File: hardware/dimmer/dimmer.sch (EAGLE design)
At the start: 34 parts, among them IC1 MEGA328PU, IC2 RFM12, IC3 7812L, IC4 LP2950Z, K1 G5LE, T1 BC547, T2 BC547, X1 AC In, X2 DIM Out, X3 AC Out

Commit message: label added
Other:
- note added: "Date: 06.04.2014"
- note removed: "Date: 05.04.2014"
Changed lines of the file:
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@@
 <frame x1="-81.28" y1="-104.14" x2="99.06" y2="91.44" columns="8" rows="5" layer="97"/>
 <text x="12.7" y="-76.2" size="3.81" layer="97">smarthomatic Dimmer</text>
-<text x="63.5" y="-81.28" size="2.1844" layer="97">Date: 05.04.2014</text>
+<text x="63.5" y="-81.28" size="2.1844" layer="97">Date: 06.04.2014</text>
 <text x="12.7" y="-81.28" size="2.1844" layer="97">Rev 1.0</text>
 <text x="12.7" y="-86.36" size="2.1844" layer="97">Copyright (c) Uwe Freese, www.smarthomatic.org</text>

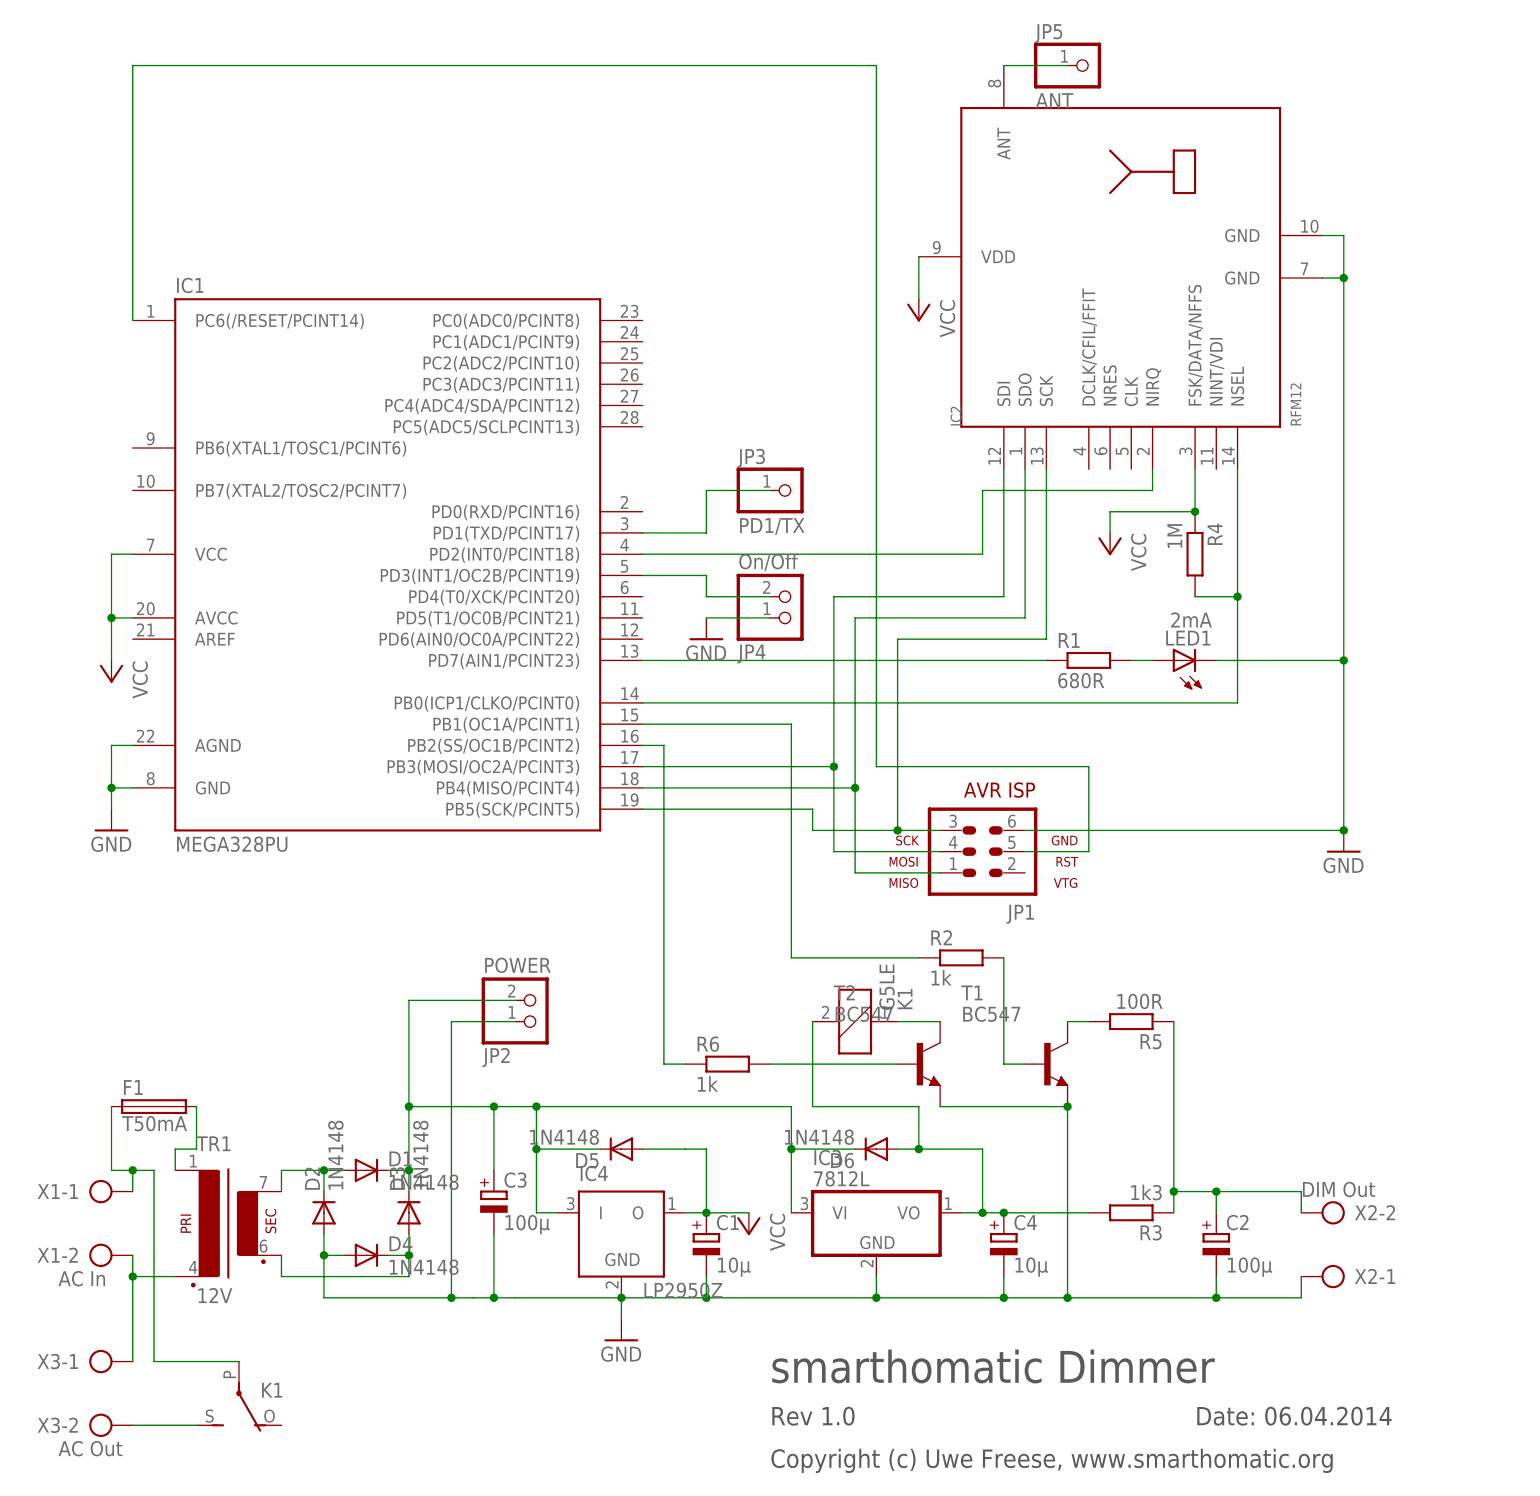
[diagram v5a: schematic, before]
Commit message: Add 220nF capacitors at ATMega + RFM12. Use more powerful transformer, also 15V now. Use smaller relay. Use 15V transformer output voltage for relay instead of regulated voltage from 78L12. Smaller PCB.
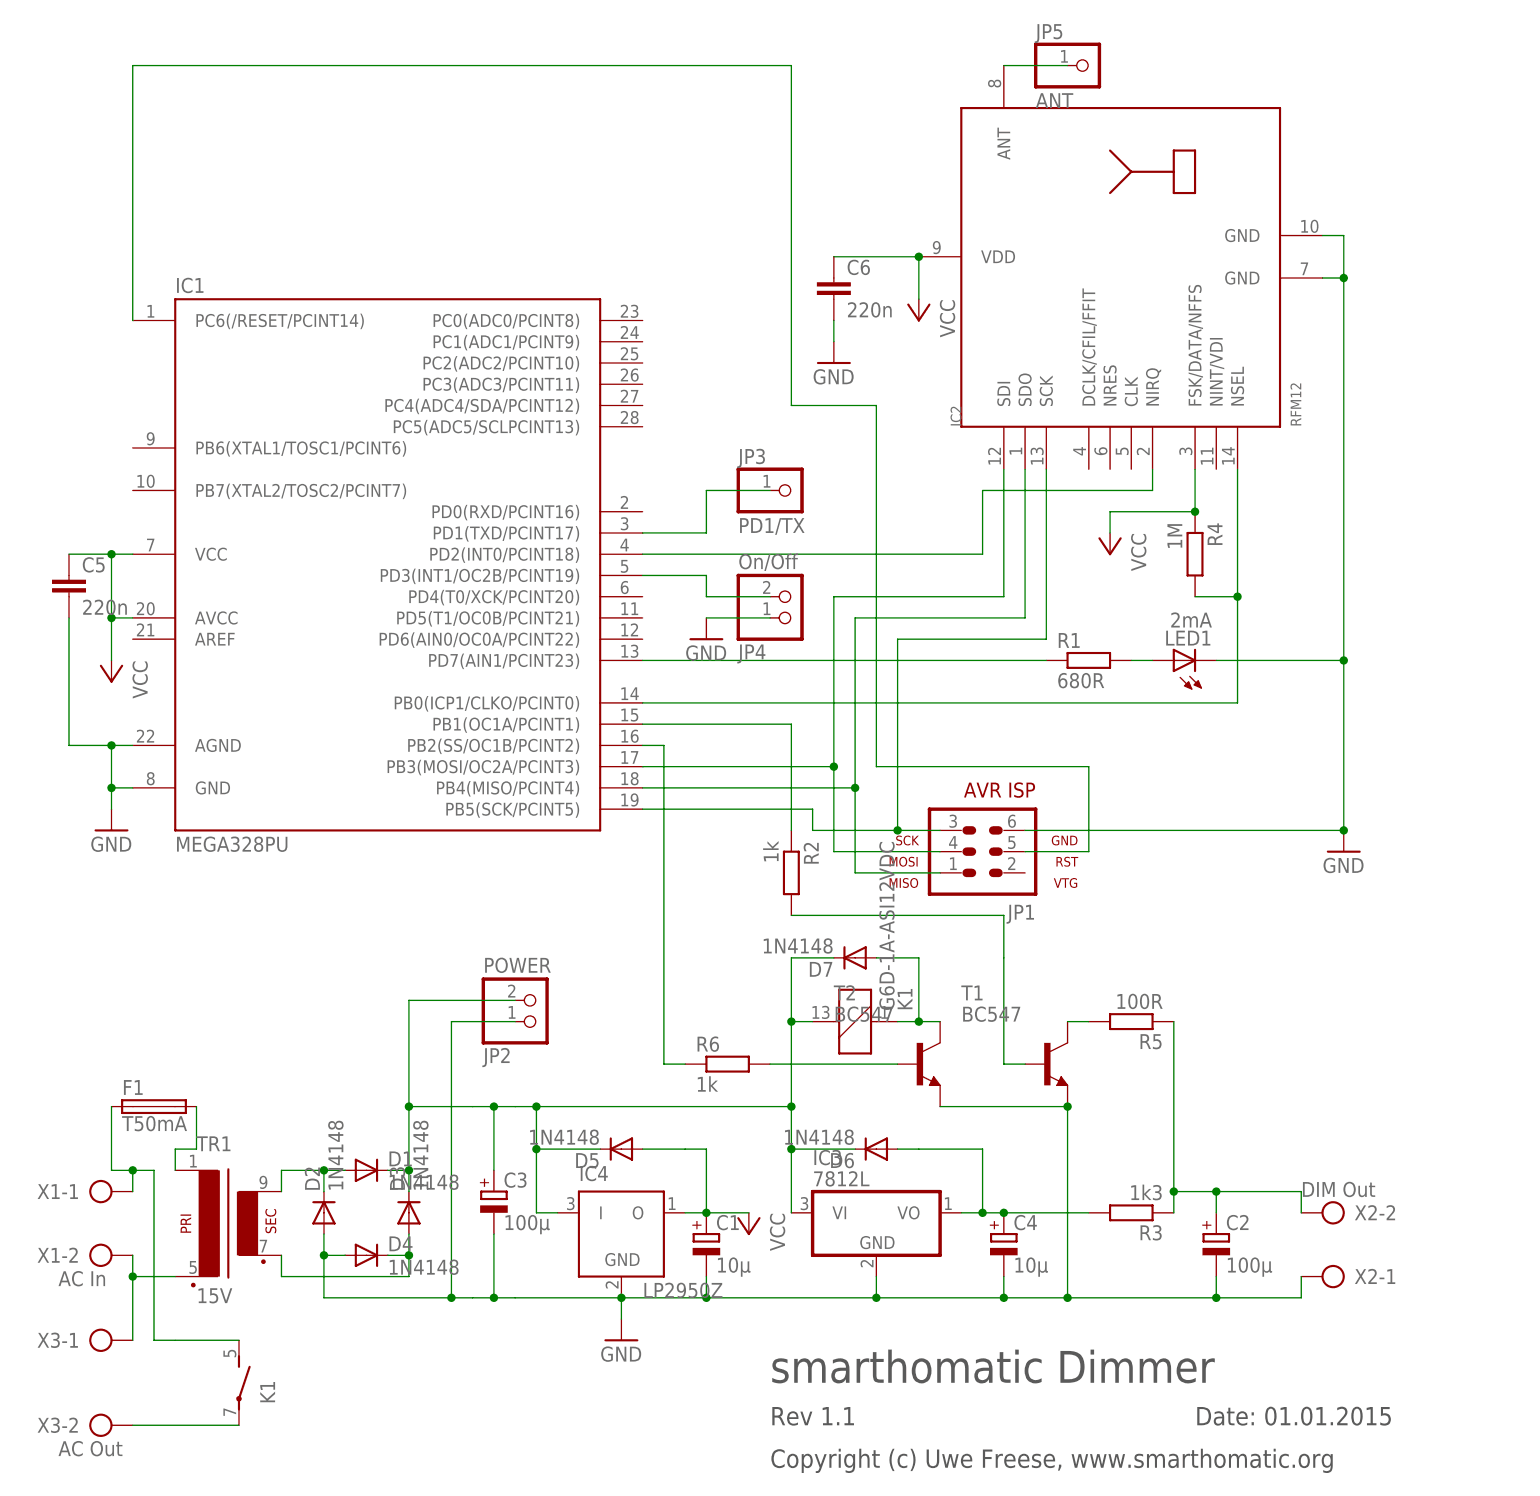
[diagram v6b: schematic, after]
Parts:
- added C5, C6: 220n, capacitor-wima:C2,5-3
- added D7: 1N4148, diode:1N4148DO35-7
- K1: value G5LE -> G6D-1A-ASI12VDC; device relay:G5LE -> relay:G6D-1A-ASI12VDC
- TR1: value 12V -> 15V; device trafo:EE20-1 -> trafo:EI30-1
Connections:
- removed net N$21: K12.S, X3-2.KL
- new net N$20: K12.P, X3-2.KL
- net GND: now also C5.2, C6.2
- net N$10: no longer K11.2
- net N$18: now also D7.A
- net N$22: now also K12.S; no longer K12.P
- net N$9: now also D7.C, K11.2
- net VCC: now also C5.1, C6.1
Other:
- note added: "Date: 01.01.2015"
- note added: "Rev 1.1"
- note removed: "Date: 06.04.2014"
- note removed: "Rev 1.0"
- moved on the sheet: K1, R2, X3-1
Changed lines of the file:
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@@
 <part name="R4" library="rcl" deviceset="R-EU_" device="0207/7" value="1M"/>
 <part name="JP5" library="pinhead" deviceset="PINHD-1X1" device="" value="ANT"/>
-<part name="TR1" library="trafo" deviceset="EE20-1" device="" value="12V"/>
+<part name="TR1" library="trafo" deviceset="EI30-1" device="" value="15V"/>
 <part name="D1" library="diode" deviceset="1N4148" device="DO35-7" value="1N4148"/>
 <part name="D2" library="diode" deviceset="1N4148" device="DO35-7" value="1N4148"/>
@@
 <attribute name="OC_NEWARK" value="unknown"/>
 </part>
-<part name="K1" library="relay" deviceset="G5LE" device=""/>
+<part name="K1" library="relay" deviceset="G6D?*" device="-1A-ASI" technology="12VDC"/>
 <part name="T2" library="transistor" deviceset="BC547" device=""/>
 <part name="R6" library="rcl" deviceset="R-EU_" device="0207/7" value="1k"/>
@@
 <part name="F1" library="fuse" deviceset="SH22,5" device="" value="T50mA"/>
 <part name="C3" library="rcl" deviceset="CPOL-EU" device="E1.8-4" value="100µ"/>
+<part name="C5" library="capacitor-wima" deviceset="C" device="2,5-3" value="220n"/>
+<part name="C6" library="capacitor-wima" deviceset="C" device="2,5-3" value="220n"/>
+<part name="GND5" library="supply1" deviceset="GND" device=""/>
+<part name="D7" library="diode" deviceset="1N4148" device="DO35-7" value="1N4148"/>
 </parts>
 <sheets>
 <sheet>
 <plain>
-<frame x1="-81.28" y1="-104.14" x2="99.06" y2="91.44" columns="8" rows="5" layer="97"/>
+<frame x1="-83.82" y1="-101.6" x2="96.52" y2="93.98" columns="8" rows="5" layer="97"/>
 <text x="12.7" y="-76.2" size="3.81" layer="97">smarthomatic Dimmer</text>
-<text x="63.5" y="-81.28" size="2.1844" layer="97">Date: 06.04.2014</text>
-<text x="12.7" y="-81.28" size="2.1844" layer="97">Rev 1.0</text>
+<text x="63.5" y="-81.28" size="2.1844" layer="97">Date: 01.01.2015</text>
+<text x="12.7" y="-81.28" size="2.1844" layer="97">Rev 1.1</text>
 <text x="12.7" y="-86.36" size="2.1844" layer="97">Copyright (c) Uwe Freese, www.smarthomatic.org</text>
 </plain>
@@
 <instance part="C1" gate="G$1" x="5.08" y="-58.42"/>
 <instance part="T1" gate="G$1" x="45.72" y="-38.1"/>
-<instance part="R2" gate="G$1" x="35.56" y="-25.4"/>
+<instance part="R2" gate="G$1" x="15.24" y="-15.24" rot="R270"/>
 <instance part="IC4" gate="G$1" x="-5.08" y="-58.42"/>
 <instance part="R3" gate="G$1" x="55.88" y="-55.88" rot="R180"/>
@@
 <instance part="D6" gate="G$1" x="25.4" y="-48.26" rot="R180"/>
 <instance part="C4" gate="G$1" x="40.64" y="-58.42"/>
-<instance part="X3" gate="-1" x="-68.58" y="-73.66"/>
+<instance part="X3" gate="-1" x="-68.58" y="-71.12"/>
 <instance part="X3" gate="-2" x="-68.58" y="-81.28"/>
 <instance part="K1" gate="1" x="22.86" y="-33.02" rot="MR90"/>
-<instance part="K1" gate="2" x="-50.8" y="-76.2" rot="MR180"/>
+<instance part="K1" gate="2" x="-50.8" y="-76.2" rot="MR0"/>
 <instance part="T2" gate="G$1" x="30.48" y="-38.1"/>
 <instance part="R6" gate="G$1" x="7.62" y="-38.1"/>
@@
 <instance part="F1" gate="1" x="-60.96" y="-43.18"/>
 <instance part="C3" gate="G$1" x="-20.32" y="-53.34"/>
+<instance part="C5" gate="G$1" x="-71.12" y="20.32"/>
+<instance part="C6" gate="G$1" x="20.32" y="55.88"/>
+<instance part="GND5" gate="1" x="20.32" y="45.72"/>
+<instance part="D7" gate="G$1" x="22.86" y="-25.4" rot="R180"/>
 </instances>
 <busses>
@@
 <wire x1="-66.04" y1="0" x2="-66.04" y2="-5.08" width="0.1524" layer="91"/>
 <junction x="-66.04" y="-5.08"/>
+<pinref part="C5" gate="G$1" pin="2"/>
+<wire x1="-66.04" y1="0" x2="-71.12" y2="0" width="0.1524" layer="91"/>
+<wire x1="-71.12" y1="0" x2="-71.12" y2="15.24" width="0.1524" layer="91"/>
+<junction x="-66.04" y="0"/>
 </segment>
 <segment>
@@
 <pinref part="GND4" gate="1" pin="GND"/>
 </segment>
+<segment>
+<pinref part="C6" gate="G$1" pin="2"/>
+<pinref part="GND5" gate="1" pin="GND"/>
+<wire x1="20.32" y1="50.8" x2="20.32" y2="48.26" width="0.1524" layer="91"/>
+</segment>
 </net>
 <net name="VCC" class="0">
@@
 <pinref part="P+3" gate="VCC" pin="VCC"/>
 <wire x1="30.48" y1="58.42" x2="30.48" y2="53.34" width="0.1524" layer="91"/>
+<pinref part="C6" gate="G$1" pin="1"/>
+<wire x1="20.32" y1="58.42" x2="30.48" y2="58.42" width="0.1524" layer="91"/>
+<junction x="30.48" y="58.42"/>
 </segment>
 <segment>
@@
 <wire x1="-66.04" y1="10.16" x2="-66.04" y2="15.24" width="0.1524" layer="91"/>
 <junction x="-66.04" y="15.24"/>
+<pinref part="C5" gate="G$1" pin="1"/>
+<wire x1="-71.12" y1="22.86" x2="-66.04" y2="22.86" width="0.1524" layer="91"/>
+<junction x="-66.04" y="22.86"/>
 </segment>
 </net>
@@
 <wire x1="50.8" y1="-12.7" x2="50.8" y2="-2.54" width="0.1524" layer="91"/>
 <wire x1="50.8" y1="-2.54" x2="25.4" y2="-2.54" width="0.1524" layer="91"/>
-<wire x1="25.4" y1="-2.54" x2="25.4" y2="81.28" width="0.1524" layer="91"/>
-<wire x1="25.4" y1="81.28" x2="-63.5" y2="81.28" width="0.1524" layer="91"/>
+<wire x1="25.4" y1="-2.54" x2="25.4" y2="40.64" width="0.1524" layer="91"/>
+<wire x1="25.4" y1="40.64" x2="15.24" y2="40.64" width="0.1524" layer="91"/>
+<wire x1="15.24" y1="40.64" x2="15.24" y2="81.28" width="0.1524" layer="91"/>
+<wire x1="15.24" y1="81.28" x2="-63.5" y2="81.28" width="0.1524" layer="91"/>
 <pinref part="IC1" gate="1" pin="PC6(/RESET/PCINT14)"/>
 <wire x1="-63.5" y1="81.28" x2="-63.5" y2="50.8" width="0.1524" layer="91"/>
@@
 <wire x1="-20.32" y1="-43.18" x2="-20.32" y2="-50.8" width="0.1524" layer="91"/>
 <junction x="-20.32" y="-43.18"/>
+<wire x1="15.24" y1="-43.18" x2="15.24" y2="-33.02" width="0.1524" layer="91"/>
+<junction x="15.24" y="-43.18"/>
+<pinref part="K1" gate="1" pin="2"/>
+<wire x1="15.24" y1="-33.02" x2="17.78" y2="-33.02" width="0.1524" layer="91"/>
+<wire x1="15.24" y1="-33.02" x2="15.24" y2="-25.4" width="0.1524" layer="91"/>
+<junction x="15.24" y="-33.02"/>
+<pinref part="D7" gate="G$1" pin="C"/>
+<wire x1="15.24" y1="-25.4" x2="20.32" y2="-25.4" width="0.1524" layer="91"/>
 </segment>
 </net>
@@
 <pinref part="R2" gate="G$1" pin="2"/>
 <pinref part="T1" gate="G$1" pin="B"/>
+<wire x1="15.24" y1="-20.32" x2="40.64" y2="-20.32" width="0.1524" layer="91"/>
+<wire x1="40.64" y1="-20.32" x2="40.64" y2="-25.4" width="0.1524" layer="91"/>
 <wire x1="40.64" y1="-25.4" x2="40.64" y2="-38.1" width="0.1524" layer="91"/>
 <wire x1="40.64" y1="-38.1" x2="43.18" y2="-38.1" width="0.1524" layer="91"/>
@@
 <junction x="40.64" y="-55.88"/>
 <wire x1="30.48" y1="-48.26" x2="27.94" y2="-48.26" width="0.1524" layer="91"/>
-<wire x1="30.48" y1="-48.26" x2="30.48" y2="-43.18" width="0.1524" layer="91"/>
-<junction x="30.48" y="-48.26"/>
-<wire x1="30.48" y1="-43.18" x2="17.78" y2="-43.18" width="0.1524" layer="91"/>
-<pinref part="K1" gate="1" pin="2"/>
-<wire x1="17.78" y1="-43.18" x2="17.78" y2="-33.02" width="0.1524" layer="91"/>
 </segment>
 </net>
@@
 <pinref part="R2" gate="G$1" pin="1"/>
 <wire x1="-2.54" y1="2.54" x2="15.24" y2="2.54" width="0.1524" layer="91"/>
-<wire x1="15.24" y1="2.54" x2="15.24" y2="-25.4" width="0.1524" layer="91"/>
-<wire x1="15.24" y1="-25.4" x2="30.48" y2="-25.4" width="0.1524" layer="91"/>
+<wire x1="15.24" y1="2.54" x2="15.24" y2="-10.16" width="0.1524" layer="91"/>
 </segment>
 </net>
@@
 <wire x1="-63.5" y1="-63.5" x2="-58.42" y2="-63.5" width="0.1524" layer="91"/>
 <pinref part="X3" gate="-1" pin="KL"/>
-<wire x1="-63.5" y1="-63.5" x2="-63.5" y2="-73.66" width="0.1524" layer="91"/>
+<wire x1="-63.5" y1="-63.5" x2="-63.5" y2="-71.12" width="0.1524" layer="91"/>
 <pinref part="X1" gate="-2" pin="KL"/>
 <wire x1="-63.5" y1="-60.96" x2="-63.5" y2="-63.5" width="0.1524" layer="91"/>
@@
 </segment>
 </net>
-<net name="N$21" class="0">
-<segment>
-<pinref part="K1" gate="2" pin="S"/>
-<pinref part="X3" gate="-2" pin="KL"/>
-<wire x1="-55.88" y1="-81.28" x2="-63.5" y2="-81.28" width="0.1524" layer="91"/>
-</segment>
-</net>
 <net name="N$22" class="0">
 <segment>
 <wire x1="-63.5" y1="-50.8" x2="-66.04" y2="-50.8" width="0.1524" layer="91"/>
 <wire x1="-63.5" y1="-50.8" x2="-60.96" y2="-50.8" width="0.1524" layer="91"/>
-<pinref part="K1" gate="2" pin="P"/>
-<wire x1="-60.96" y1="-73.66" x2="-50.8" y2="-73.66" width="0.1524" layer="91"/>
-<wire x1="-60.96" y1="-50.8" x2="-60.96" y2="-73.66" width="0.1524" layer="91"/>
+<wire x1="-60.96" y1="-50.8" x2="-60.96" y2="-71.12" width="0.1524" layer="91"/>
 <pinref part="X1" gate="-1" pin="KL"/>
 <wire x1="-63.5" y1="-53.34" x2="-63.5" y2="-50.8" width="0.1524" layer="91"/>
@@
 <pinref part="F1" gate="1" pin="1"/>
 <wire x1="-66.04" y1="-50.8" x2="-66.04" y2="-43.18" width="0.1524" layer="91"/>
+<pinref part="K1" gate="2" pin="S"/>
+<wire x1="-50.8" y1="-71.12" x2="-58.42" y2="-71.12" width="0.1524" layer="91"/>
+<wire x1="-58.42" y1="-71.12" x2="-60.96" y2="-71.12" width="0.1524" layer="91"/>
 </segment>
 </net>
@@
 <pinref part="K1" gate="1" pin="1"/>
 <pinref part="T2" gate="G$1" pin="C"/>
-<wire x1="27.94" y1="-33.02" x2="33.02" y2="-33.02" width="0.1524" layer="91"/>
+<wire x1="27.94" y1="-33.02" x2="30.48" y2="-33.02" width="0.1524" layer="91"/>
+<wire x1="30.48" y1="-33.02" x2="33.02" y2="-33.02" width="0.1524" layer="91"/>
+<wire x1="30.48" y1="-33.02" x2="30.48" y2="-25.4" width="0.1524" layer="91"/>
+<junction x="30.48" y="-33.02"/>
+<pinref part="D7" gate="G$1" pin="A"/>
+<wire x1="30.48" y1="-25.4" x2="25.4" y2="-25.4" width="0.1524" layer="91"/>
 </segment>
 </net>
@@
 </segment>
 </net>
+<net name="N$20" class="0">
+<segment>
+<pinref part="X3" gate="-2" pin="KL"/>
+<pinref part="K1" gate="2" pin="P"/>
+<wire x1="-63.5" y1="-81.28" x2="-50.8" y2="-81.28" width="0.1524" layer="91"/>
+</segment>
+</net>

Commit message: Add solder jumper for ISP VCC.
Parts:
- added SJ1: ISP VCC, jumper:SJW
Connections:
- new net N$21: JP1.2, SJ1.1
- net VCC: now also SJ1.2
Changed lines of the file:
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@@
 <part name="GND5" library="supply1" deviceset="GND" device=""/>
 <part name="D7" library="diode" deviceset="1N4148" device="DO35-7" value="1N4148"/>
+<part name="SJ1" library="jumper" deviceset="SJ" device="W" value="ISP VCC"/>
+<part name="P+5" library="supply1" deviceset="VCC" device=""/>
 </parts>
 <sheets>
@@
 <instance part="GND5" gate="1" x="20.32" y="45.72"/>
 <instance part="D7" gate="G$1" x="22.86" y="-25.4" rot="R180"/>
+<instance part="SJ1" gate="1" x="58.42" y="-15.24"/>
+<instance part="P+5" gate="VCC" x="66.04" y="-17.78" rot="R180"/>
 </instances>
 <busses>
@@
 <junction x="-66.04" y="22.86"/>
 </segment>
+<segment>
+<pinref part="SJ1" gate="1" pin="2"/>
+<pinref part="P+5" gate="VCC" pin="VCC"/>
+<wire x1="63.5" y1="-15.24" x2="66.04" y2="-15.24" width="0.1524" layer="91"/>
+</segment>
 </net>
 <net name="N$3" class="0">
@@
 </segment>
 </net>
+<net name="N$21" class="0">
+<segment>
+<pinref part="JP1" gate="G$1" pin="2"/>
+<pinref part="SJ1" gate="1" pin="1"/>
+<wire x1="43.18" y1="-15.24" x2="53.34" y2="-15.24" width="0.1524" layer="91"/>
+</segment>
+</net>

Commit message: Change SMD solder pad.
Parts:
- SJ1: device jumper:SJW -> jumper:SJ
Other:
- note added: "Date: 02.01.2015"
- note added: "Rev 1.2"
- note removed: "Date: 01.01.2015"
- note removed: "Rev 1.1"
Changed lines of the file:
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@@
 <part name="GND5" library="supply1" deviceset="GND" device=""/>
 <part name="D7" library="diode" deviceset="1N4148" device="DO35-7" value="1N4148"/>
-<part name="SJ1" library="jumper" deviceset="SJ" device="W" value="ISP VCC"/>
+<part name="SJ1" library="jumper" deviceset="SJ" device="" value="ISP VCC"/>
 <part name="P+5" library="supply1" deviceset="VCC" device=""/>
 </parts>
@@
 <frame x1="-83.82" y1="-101.6" x2="96.52" y2="93.98" columns="8" rows="5" layer="97"/>
 <text x="12.7" y="-76.2" size="3.81" layer="97">smarthomatic Dimmer</text>
-<text x="63.5" y="-81.28" size="2.1844" layer="97">Date: 01.01.2015</text>
-<text x="12.7" y="-81.28" size="2.1844" layer="97">Rev 1.1</text>
+<text x="63.5" y="-81.28" size="2.1844" layer="97">Date: 02.01.2015</text>
+<text x="12.7" y="-81.28" size="2.1844" layer="97">Rev 1.2</text>
 <text x="12.7" y="-86.36" size="2.1844" layer="97">Copyright (c) Uwe Freese, www.smarthomatic.org</text>
 </plain>
